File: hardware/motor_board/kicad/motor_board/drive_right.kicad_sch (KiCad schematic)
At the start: 20 parts, among them U4 DRV8316CRRGFR

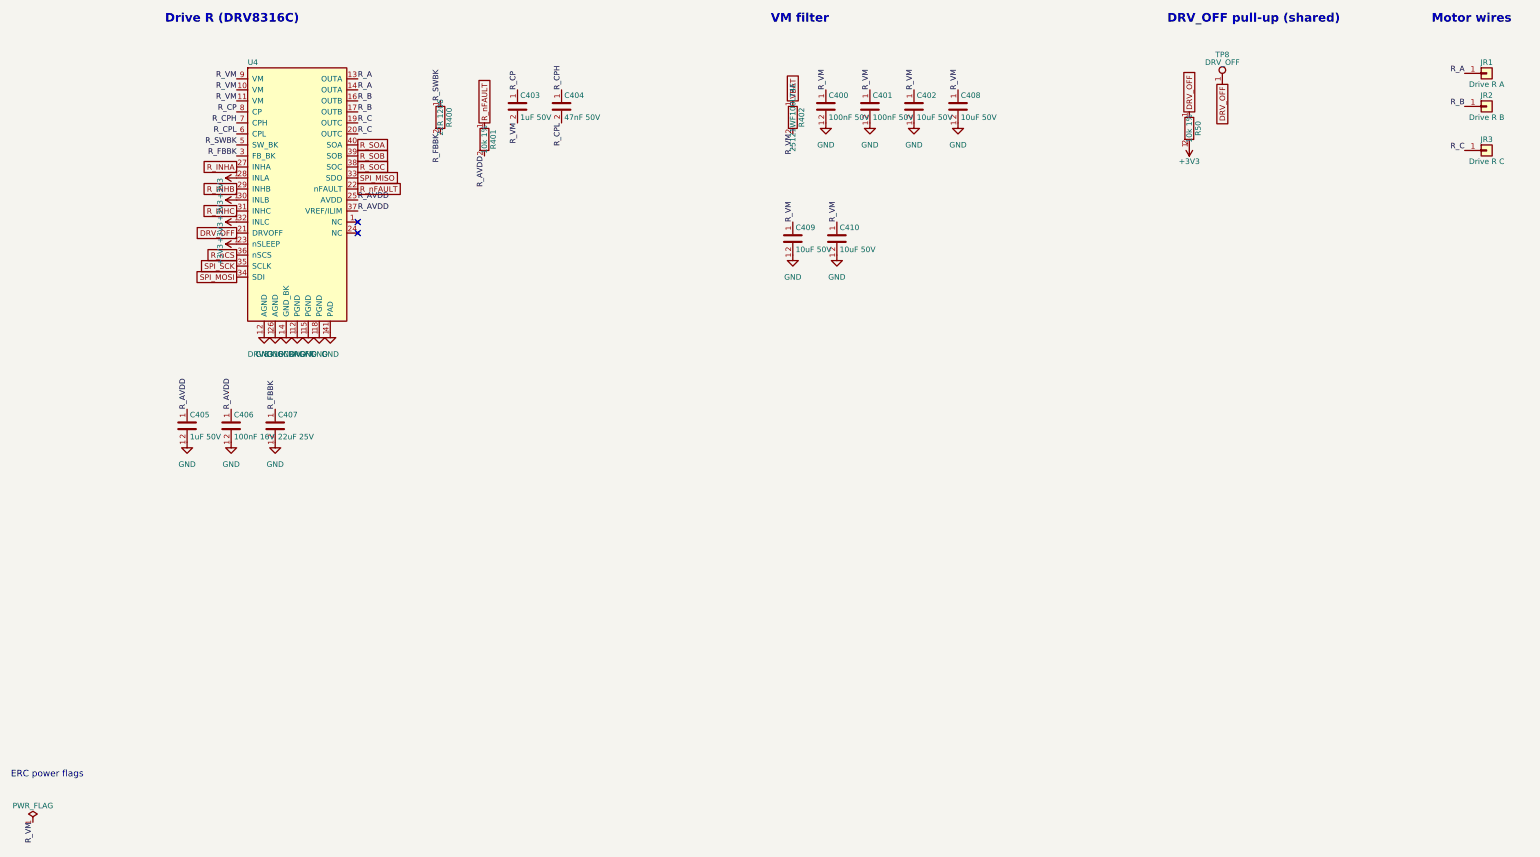
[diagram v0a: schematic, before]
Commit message: v2 package swaps (rev L2), after adversarial review: U6 WQFN-14 (EP to GND), D2 PMEG4030ER, L1 ZEMS404030 4.1 mm, J4 vertical XH, J2/J3 genuine JST vertical SH, R300/R400 0603 anti-surge, R15/C14/D10 one size down; drive VM bulk 2 x 10 uF X7R 1210 per drive (C309/C310/C409/C410 removed, user OK) - the 1206 X5R kept only ~2.3 uF at 16.8 V
sim_hotplug.py models MLCC DC bias (worst bounce 2.14 V/us at 0 C, 2.62 at -40 C); library check 0 errors, mutation test all caught; schematic regenerated, nets 176/176; v2 board rebuilt: DRC 0, parity 0; WQFN-14 3D model generated; DESIGN/calcs/BOM/FAB/CHANGES updated (CPL rotation fix for J2/J3/J4)

Co-Authored-By: Claude Opus 5.5 (1M context) <noreply@anthropic.com>
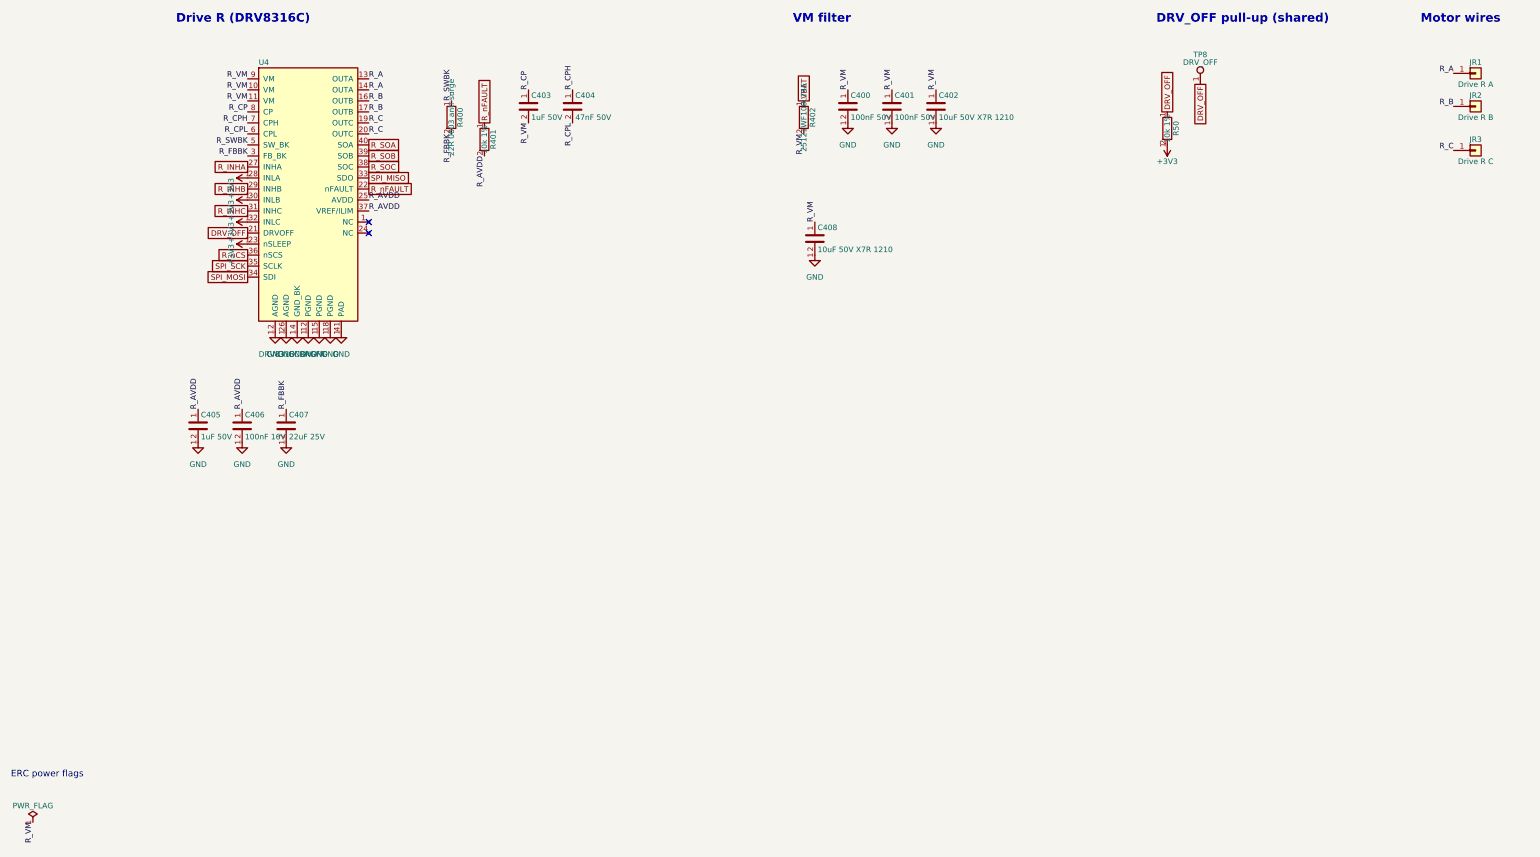
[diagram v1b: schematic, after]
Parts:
- removed C409, C410: 10uF 50V, Capacitor_SMD:C_1206_3216Metric, symbol Device:C
- C402, C408: value 10uF 50V -> 10uF 50V X7R 1210; footprint Capacitor_SMD:C_1206_3216Metric -> Capacitor_SMD:C_1210_3225Metric; LCSC C13585 -> C77102
- R400: value 22R 1206 -> 22R 0603 anti-surge; footprint Resistor_SMD:R_1206_3216Metric -> Resistor_SMD:R_0603_1608Metric; LCSC C17958 -> C2074038
